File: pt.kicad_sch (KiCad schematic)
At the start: 13 parts, among them J30 PT

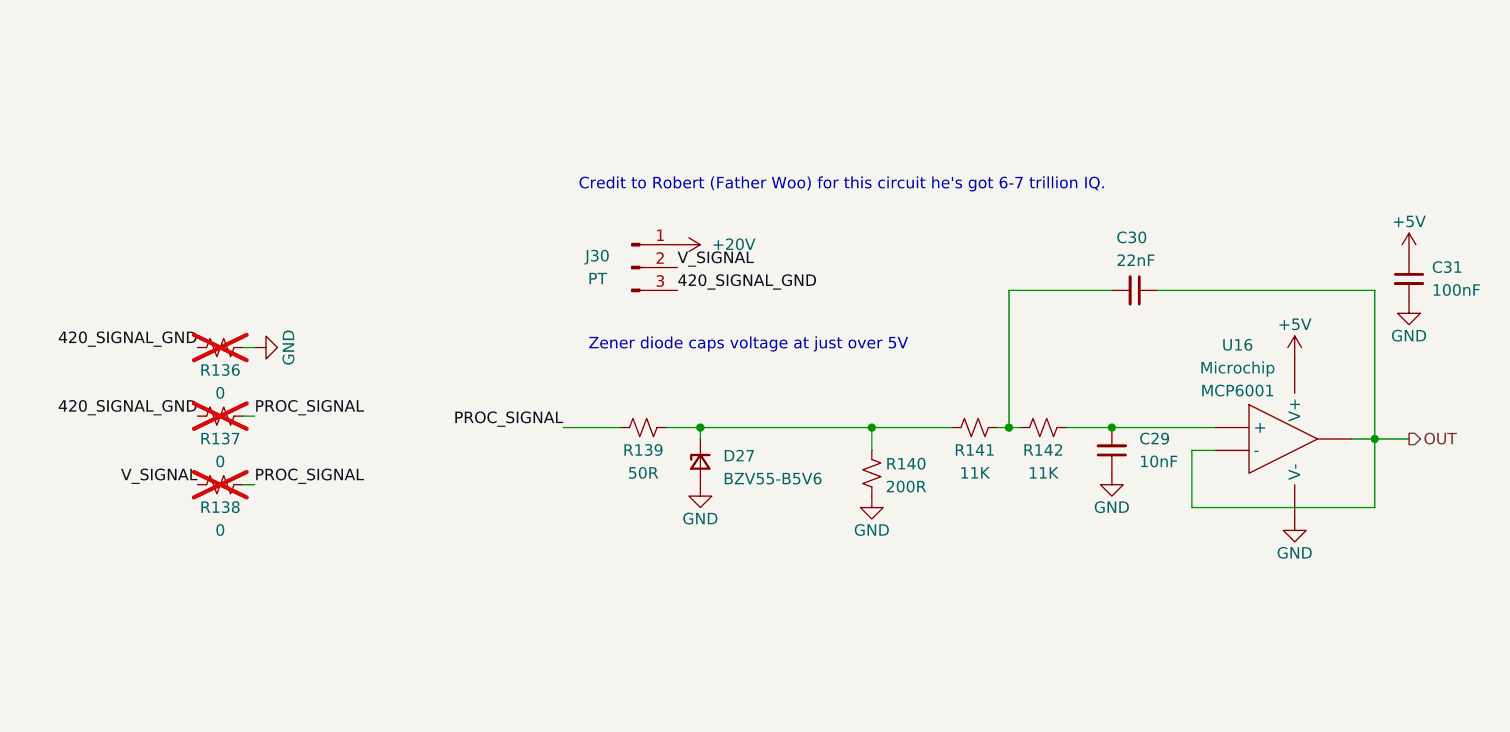
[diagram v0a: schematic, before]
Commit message: GSE v2.1: Updates for DSUB connectors for schematic only done. Layout needs a ton of work
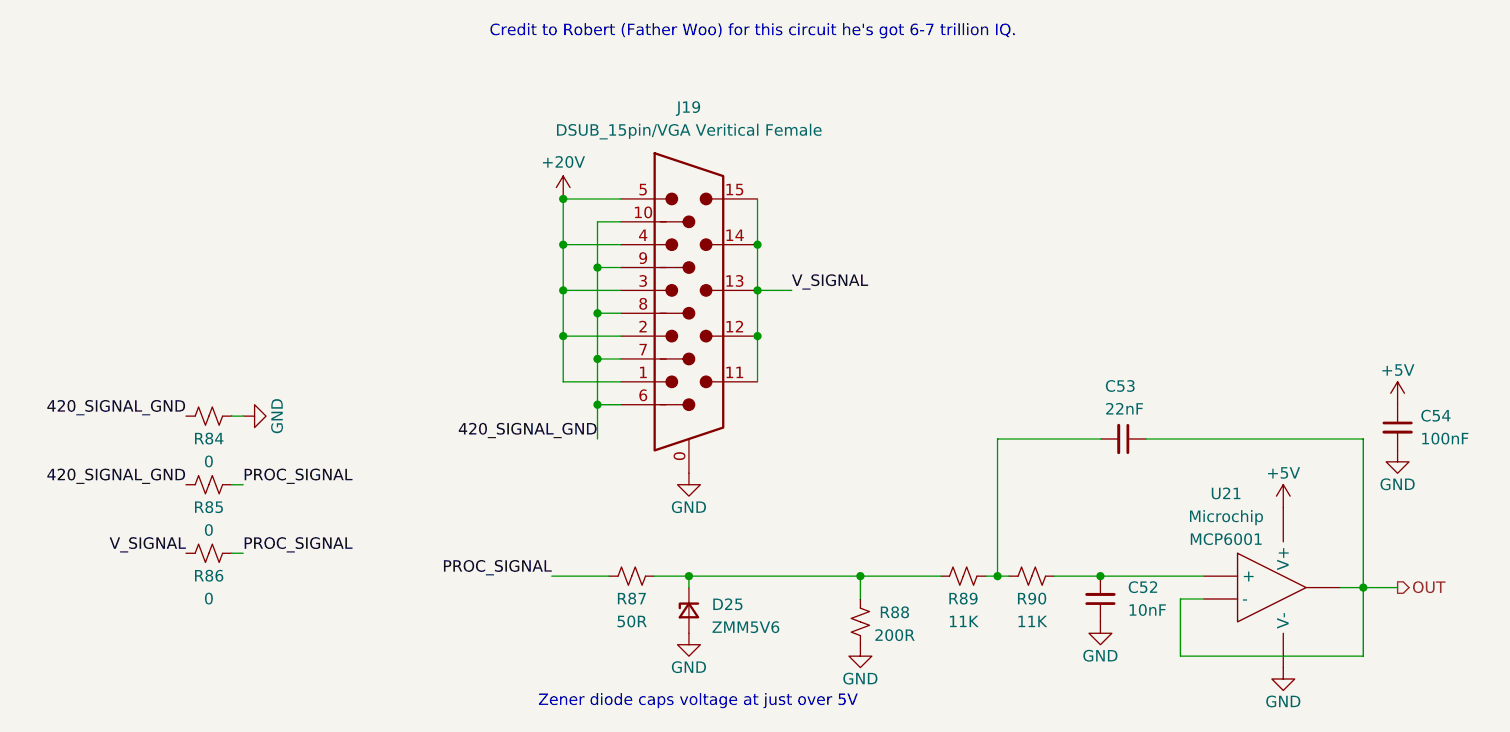
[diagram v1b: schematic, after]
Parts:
- removed J30: PT, 0UCIRP-KiCAD-Lib:GX-12 3 pin, symbol Connector:Conn_01x03_Pin
- added J19: DSUB_15pin/VGA Veritical Female, 0UCIRP-KiCAD-Lib:Connector_VGA_Vertical, symbol 0UCIRP-KiCAD-Lib:Connector_VGA_vertical
- D25: renamed from D27; value BZV55-B5V6 -> ZMM5V6
- R84: renamed from R136; now fitted
- R85: renamed from R137; now fitted
- R86: renamed from R138; now fitted
- U21: renamed from U16; value ~ -> MCP6001
- renumbered C29 to C52, C30 to C53, C31 to C54, R139 to R87, R140 to R88, R141 to R89, R142 to R90
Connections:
- net +20V: now also J19.1, J19.2, J19.3, J19.4, J19.5
- net 420_SIGNAL_GND: now also J19.10, J19.6, J19.7, J19.8, J19.9
- net GND: now also J19.0
- net V_SIGNAL: now also J19.11, J19.12, J19.13, J19.14, J19.15
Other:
- moved on the sheet: C52, C53, C54, D25, R87, R88, R89, R90, U21

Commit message: GSE v2.1 done, just waiting on prop rn to finalize their sensor list
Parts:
- removed U21: MCP6001, Package_TO_SOT_SMD:SOT-23-5, symbol UCIRP-KiCAD-Lib:MCP6001
- added U21: MCP6001, 0UCIRP-KiCAD-Lib:Op-amp MCP6001, symbol 0UCIRP-KiCAD-Lib:Op-amp MCP6001
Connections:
- net +5V: now also U21.5 (V+)
- net GND: now also U21.2 (V-)
- net OUT: now also U21.1, U21.4 (-)
- net at C52.2, R90.1: now also U21.3 (+)

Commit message: GSE v2.1: small changes made and typos
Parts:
- J19: value DSUB_15pin/VGA Veritical Female -> DSUB_15pin/VGA Vertical Female
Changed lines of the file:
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@@
 			)
 		)
-		(property "Value" "DSUB_15pin/VGA Veritical  Female"
+		(property "Value" "DSUB_15pin/VGA Vertical  Female"
 			(at 115.57 81.28 0)
 			(effects

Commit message: GSEv2.1: changed pinout for PT and Loadcell where pin11 on VGA is grounded
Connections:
- net GND: now also J19.11
- net V_SIGNAL: no longer J19.11
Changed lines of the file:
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@@
 	)
 	(junction
-		(at 123.19 104.14)
+		(at 115.57 119.38)
 		(diameter 0)
 		(color 0 0 0 0)
@@
 	(wire
 		(pts
-			(xy 123.19 104.14) (xy 123.19 109.22)
+			(xy 123.19 119.38) (xy 115.57 119.38)
 		)
 		(stroke
@@
 		)
 		(stroke
+			(width 0)
+			(type default)
+		)
+	)
+	(wire
+		(pts
+			(xy 123.19 109.22) (xy 123.19 119.38)
+		)
+		(stroke

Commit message: GSE v2.1: Done, ready for JLCPCB
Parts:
- renumbered D25 to D28, R84 to R87, R85 to R88, R86 to R89, R87 to R90, R88 to R91, R89 to R92, R90 to R93
